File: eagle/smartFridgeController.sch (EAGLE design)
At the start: 12 parts

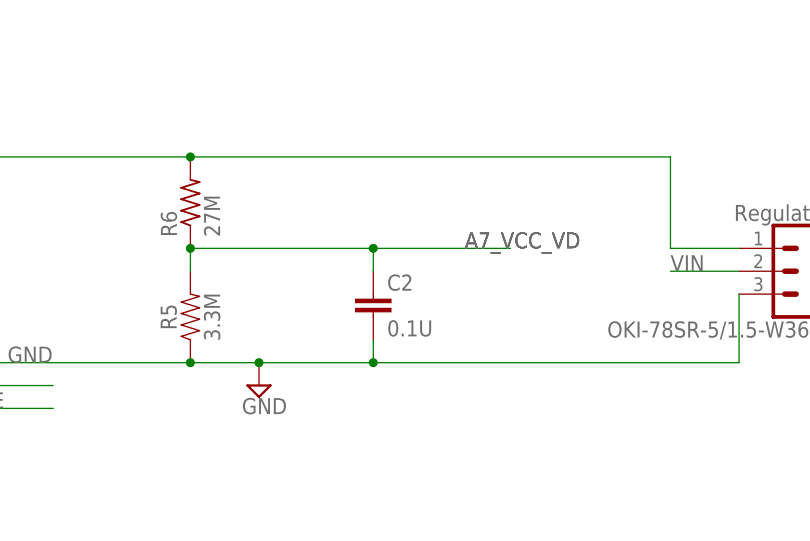
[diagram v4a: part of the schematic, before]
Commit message: silkscreen updates
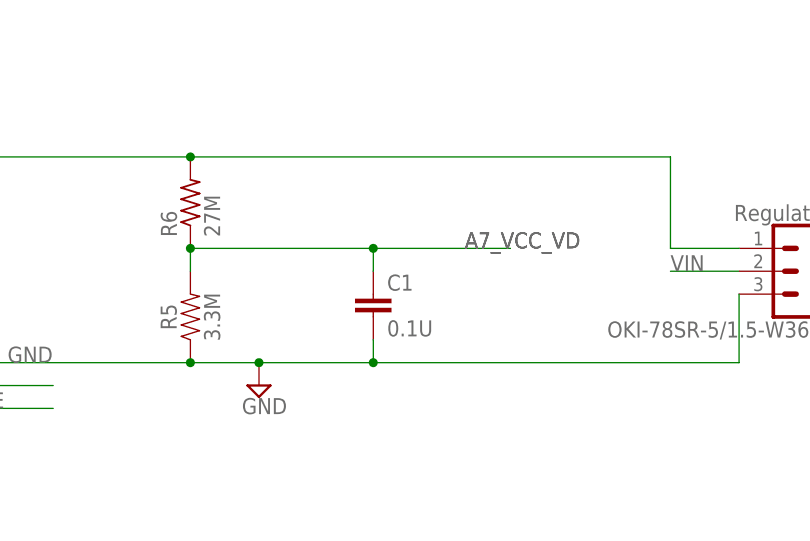
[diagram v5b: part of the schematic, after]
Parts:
- renumbered C2 to C1
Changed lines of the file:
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@@
 <part name="FRAME1" library="SparkFun-Aesthetics" deviceset="FRAME-A4L" device=""/>
 <part name="SUPPLY7" library="supply2" deviceset="GND" device=""/>
-<part name="C2" library="SparkFun-Capacitors" deviceset="0.1UF" device="-KIT-EZ-50V-20%" value="0.1U"/>
+<part name="C1" library="SparkFun-Capacitors" deviceset="0.1UF" device="-KIT-EZ-50V-20%" value="0.1U"/>
 <part name="R5" library="SparkFun-Resistors" deviceset="1KOHM" device="-HORIZ-1/4W-1%" value="3.3M"/>
 <part name="JST" library="SparkFun-Connectors" deviceset="CONN_04" device="JST-PTH"/>
@@
 <instance part="FRAME1" gate="G$1" x="0" y="0"/>
 <instance part="SUPPLY7" gate="GND" x="177.8" y="43.18"/>
-<instance part="C2" gate="G$1" x="190.5" y="50.8"/>
+<instance part="C1" gate="G$1" x="190.5" y="50.8"/>
 <instance part="R5" gate="G$1" x="170.18" y="50.8" rot="R90"/>
 <instance part="JST" gate="G$1" x="139.7" y="43.18"/>
@@
 <net name="GND" class="1">
 <segment>
-<pinref part="C2" gate="G$1" pin="2"/>
+<pinref part="C1" gate="G$1" pin="2"/>
 <wire x1="144.78" y1="45.72" x2="170.18" y2="45.72" width="0.1524" layer="91"/>
 <wire x1="170.18" y1="45.72" x2="177.8" y2="45.72" width="0.1524" layer="91"/>
@@
 </segment>
 <segment>
-<pinref part="C2" gate="G$1" pin="1"/>
+<pinref part="C1" gate="G$1" pin="1"/>
 <pinref part="R5" gate="G$1" pin="2"/>
 <wire x1="190.5" y1="55.88" x2="190.5" y2="58.42" width="0.1524" layer="91"/>

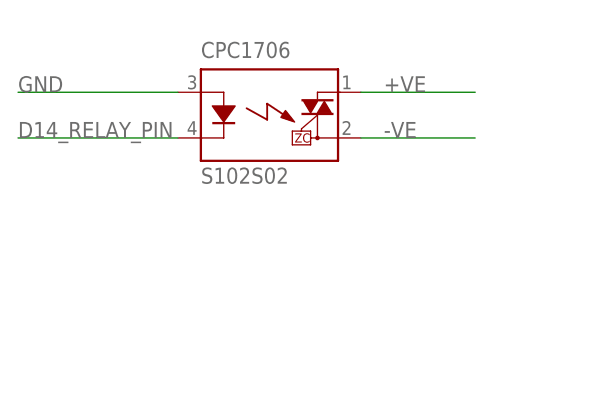
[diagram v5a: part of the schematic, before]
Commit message: Swapped IXYS pins
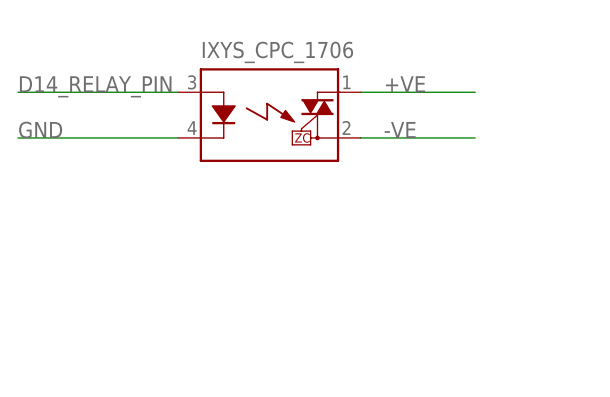
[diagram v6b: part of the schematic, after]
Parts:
- renumbered CPC1706 to IXYS_CPC_1706
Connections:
- net D14_RELAY_PIN: now also IXYS_CPC_1706.A; no longer IXYS_CPC_1706.K
- net GND: now also IXYS_CPC_1706.K; no longer IXYS_CPC_1706.A
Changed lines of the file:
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@@
 <schematic xreflabel="%F%N/%S.%C%R" xrefpart="/%S.%C%R">
 <attributes>
-<attribute name="CNAME" value="MoteinoMega ABoatMon GPS Shield"/>
-<attribute name="CREVISION" value="2.99"/>
+<attribute name="CNAME" value="Smat Fridge Controller"/>
+<attribute name="CREVISION" value="0.2"/>
 <attribute name="DESIGNER" value="greg.cope@gmail.com"/>
 </attributes>
@@
 <part name="SUPPLY3" library="supply2" deviceset="GND" device=""/>
 <part name="OKI-78SR-5/1.5-W36-C" library="SparkFun-Connectors" deviceset="CONN_03" device="" value="Regulator"/>
-<part name="CPC1706" library="relay" library_urn="urn:adsk.eagle:library:339" deviceset="S*02S02" device="" package3d_urn="urn:adsk.eagle:package:24541/1" technology="1"/>
+<part name="IXYS_CPC_1706" library="relay" library_urn="urn:adsk.eagle:library:339" deviceset="S*02S02" device="" package3d_urn="urn:adsk.eagle:package:24541/1" technology="1"/>
 <part name="18B20" library="SparkFun-Connectors" deviceset="CONN_06" device="SILK_FEMALE_PTH"/>
 <part name="DZ1" library="led" library_urn="urn:adsk.eagle:library:259" deviceset="LZR183" device="" package3d_urn="urn:adsk.eagle:package:15788/1"/>
@@
 <instance part="SUPPLY3" gate="GND" x="124.46" y="73.66"/>
 <instance part="OKI-78SR-5/1.5-W36-C" gate="J$1" x="238.76" y="55.88" rot="R180"/>
-<instance part="CPC1706" gate="G$1" x="48.26" y="147.32"/>
+<instance part="IXYS_CPC_1706" gate="G$1" x="48.26" y="147.32" smashed="yes">
+<attribute name="NAME" x="40.64" y="153.67" size="1.778" layer="95" font="vector"/>
+</instance>
 <instance part="18B20" gate="G$1" x="106.68" y="144.78"/>
 <instance part="DZ1" gate="-1" x="228.6" y="121.92" rot="R90"/>
@@
 </segment>
 <segment>
-<pinref part="CPC1706" gate="G$1" pin="A"/>
-<wire x1="38.1" y1="149.86" x2="20.32" y2="149.86" width="0.1524" layer="91"/>
-<label x="20.32" y="149.86" size="1.778" layer="95"/>
-</segment>
-<segment>
 <pinref part="18B20" gate="G$1" pin="4"/>
 <wire x1="111.76" y1="147.32" x2="124.46" y2="147.32" width="0.1524" layer="91"/>
@@
 <wire x1="233.68" y1="147.32" x2="238.76" y2="147.32" width="0.1524" layer="91"/>
 <pinref part="SUPPLY4" gate="GND" pin="GND"/>
+</segment>
+<segment>
+<pinref part="IXYS_CPC_1706" gate="G$1" pin="K"/>
+<wire x1="38.1" y1="144.78" x2="20.32" y2="144.78" width="0.1524" layer="91"/>
+<label x="20.32" y="144.78" size="1.778" layer="95"/>
 </segment>
 </net>
@@
 </segment>
 <segment>
-<pinref part="CPC1706" gate="G$1" pin="DS1"/>
+<pinref part="IXYS_CPC_1706" gate="G$1" pin="DS1"/>
 <wire x1="58.42" y1="149.86" x2="71.12" y2="149.86" width="0.1524" layer="91"/>
 <label x="60.96" y="149.86" size="1.778" layer="95"/>
@@
 </segment>
 <segment>
-<pinref part="CPC1706" gate="G$1" pin="DS2"/>
+<pinref part="IXYS_CPC_1706" gate="G$1" pin="DS2"/>
 <wire x1="58.42" y1="144.78" x2="71.12" y2="144.78" width="0.1524" layer="91"/>
 <label x="60.96" y="144.78" size="1.778" layer="95"/>
@@
 </segment>
 <segment>
-<pinref part="CPC1706" gate="G$1" pin="K"/>
-<wire x1="38.1" y1="144.78" x2="20.32" y2="144.78" width="0.1524" layer="91"/>
-<label x="20.32" y="144.78" size="1.778" layer="95"/>
-</segment>
-</net>
+<pinref part="IXYS_CPC_1706" gate="G$1" pin="A"/>
+<wire x1="38.1" y1="149.86" x2="20.32" y2="149.86" width="0.1524" layer="91"/>
+<label x="20.32" y="149.86" size="1.778" layer="95"/>
+</segment>
+</net>

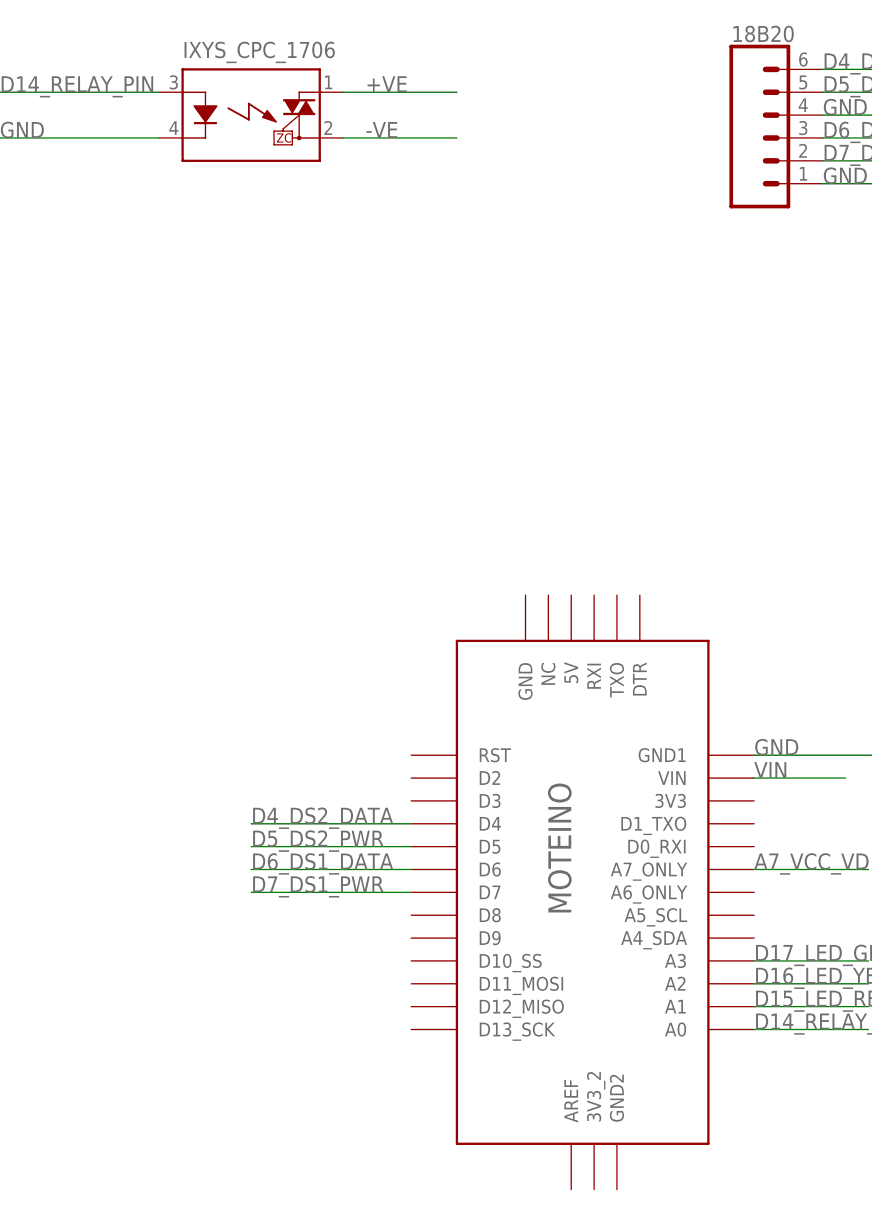
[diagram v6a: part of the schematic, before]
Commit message: Correct SIP package, large footprint
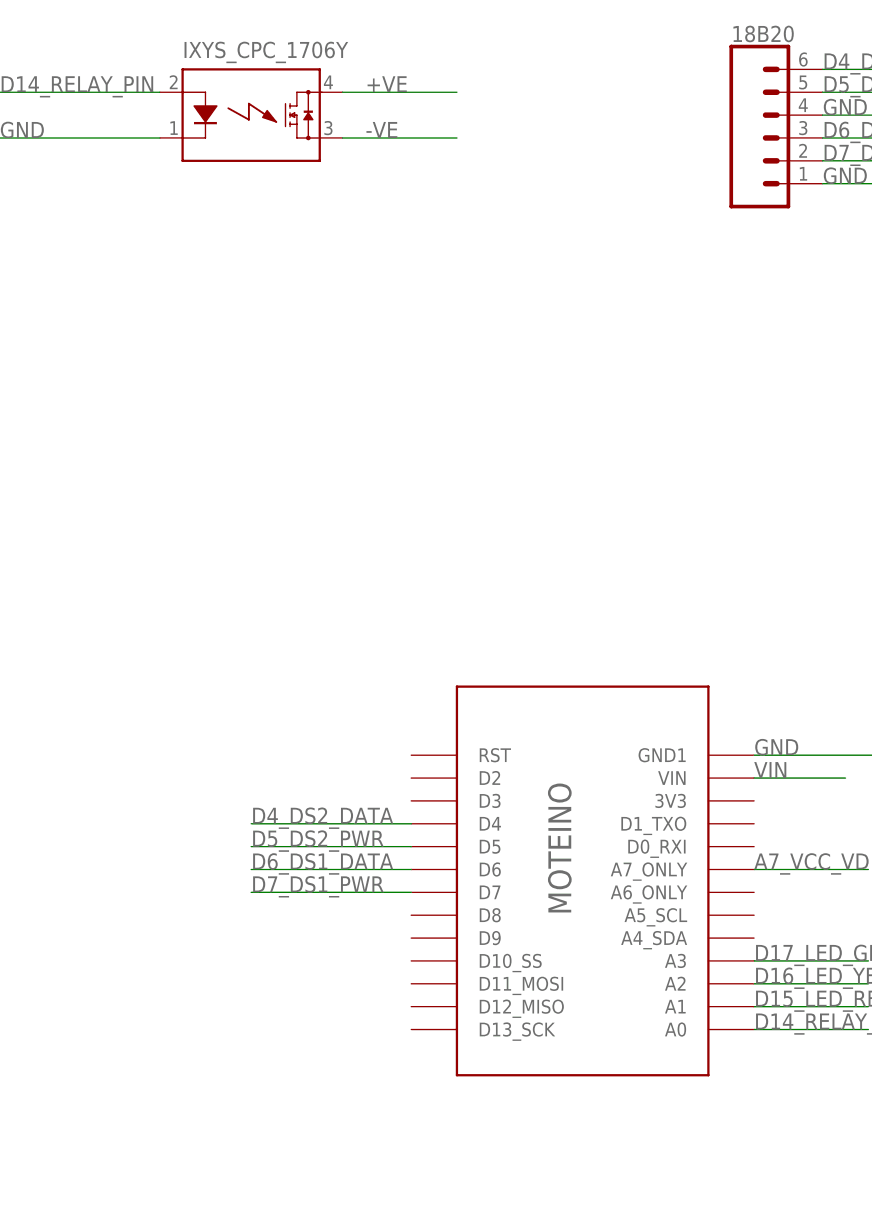
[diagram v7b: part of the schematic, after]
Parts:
- removed IXYS_CPC_1706: S102S02, relay:S102S02
- removed U$1: MOTEINOR6, Moteino:MOTEINOR6
- added IXYS_CPC_1706Y: AQZ102D, relay:AQZ102D
- added U$2: MOTEINO_SIMPLE, Moteino:MOTEINO_SIMPLE
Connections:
- net +VE: now also IXYS_CPC_1706Y.DS1; no longer IXYS_CPC_1706.DS1
- net -VE: now also IXYS_CPC_1706Y.DS2; no longer IXYS_CPC_1706.DS2
- net A7_VCC_VD: now also U$2.A7_ONLY; no longer U$1.A7_ONLY
- net D14_RELAY_PIN: now also IXYS_CPC_1706Y.A, U$2.A0; no longer IXYS_CPC_1706.A, U$1.A0
- net D15_LED_RED_PIN: now also U$2.A1; no longer U$1.A1
- net D16_LED_YELLOW_PIN: now also U$2.A2; no longer U$1.A2
- net D17_LED_GREEN_PIN: now also U$2.A3; no longer U$1.A3
- net D4_DS2_DATA: now also U$2.D4; no longer U$1.D4
- net D5_DS2_PWR: now also U$2.D5; no longer U$1.D5
- net D6_DS1_DATA: now also U$2.D6; no longer U$1.D6
- net D7_DS1_PWR: now also U$2.D7; no longer U$1.D7
- net GND: now also IXYS_CPC_1706Y.K, U$2.GND1; no longer IXYS_CPC_1706.K
- net VIN: now also U$2.VIN; no longer U$1.VIN
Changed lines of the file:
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@@
 <attributes>
 <attribute name="CNAME" value="Smat Fridge Controller"/>
-<attribute name="CREVISION" value="0.2"/>
+<attribute name="CREVISION" value="0.3"/>
 <attribute name="DESIGNER" value="greg.cope@gmail.com"/>
 </attributes>
@@
 <part name="JST" library="SparkFun-Connectors" deviceset="CONN_04" device="JST-PTH"/>
 <part name="R6" library="adafruit" deviceset="R-US_" device="0309/12" value="27M"/>
-<part name="U$1" library="Moteino" deviceset="MOTEINO" device="R6"/>
 <part name="SUPPLY3" library="supply2" deviceset="GND" device=""/>
 <part name="OKI-78SR-5/1.5-W36-C" library="SparkFun-Connectors" deviceset="CONN_03" device="" value="Regulator"/>
-<part name="IXYS_CPC_1706" library="relay" library_urn="urn:adsk.eagle:library:339" deviceset="S*02S02" device="" package3d_urn="urn:adsk.eagle:package:24541/1" technology="1"/>
 <part name="18B20" library="SparkFun-Connectors" deviceset="CONN_06" device="SILK_FEMALE_PTH"/>
 <part name="DZ1" library="led" library_urn="urn:adsk.eagle:library:259" deviceset="LZR183" device="" package3d_urn="urn:adsk.eagle:package:15788/1"/>
@@
 <part name="SUPPLY2" library="supply2" deviceset="GND" device=""/>
 <part name="SUPPLY4" library="supply2" deviceset="GND" device=""/>
+<part name="U$2" library="Moteino" deviceset="MOTEINO_SIMPLE" device=""/>
+<part name="IXYS_CPC_1706Y" library="relay" library_urn="urn:adsk.eagle:library:339" deviceset="AQZ10*D" device="" package3d_urn="urn:adsk.eagle:package:24370/1" technology="2"/>
 </parts>
 <sheets>
@@
 <instance part="JST" gate="G$1" x="139.7" y="43.18"/>
 <instance part="R6" gate="G$1" x="170.18" y="63.5" rot="R90"/>
-<instance part="U$1" gate="G$1" x="81.28" y="58.42"/>
 <instance part="SUPPLY3" gate="GND" x="124.46" y="73.66"/>
 <instance part="OKI-78SR-5/1.5-W36-C" gate="J$1" x="238.76" y="55.88" rot="R180"/>
-<instance part="IXYS_CPC_1706" gate="G$1" x="48.26" y="147.32" smashed="yes">
-<attribute name="NAME" x="40.64" y="153.67" size="1.778" layer="95" font="vector"/>
-</instance>
 <instance part="18B20" gate="G$1" x="106.68" y="144.78"/>
 <instance part="DZ1" gate="-1" x="228.6" y="121.92" rot="R90"/>
@@
 <instance part="SUPPLY2" gate="GND" x="241.3" y="134.62" rot="R90"/>
 <instance part="SUPPLY4" gate="GND" x="241.3" y="147.32" rot="R90"/>
+<instance part="U$2" gate="G$1" x="81.28" y="58.42"/>
+<instance part="IXYS_CPC_1706Y" gate="G$1" x="48.26" y="147.32" smashed="yes">
+<attribute name="NAME" x="40.64" y="153.67" size="1.778" layer="95" font="vector"/>
+</instance>
 </instances>
 <busses>
@@
 <wire x1="124.46" y1="76.2" x2="104.14" y2="76.2" width="0.1524" layer="91"/>
 <label x="104.14" y="76.2" size="1.778" layer="95"/>
+<pinref part="U$2" gate="G$1" pin="GND1"/>
 </segment>
 <segment>
@@
 </segment>
 <segment>
-<pinref part="IXYS_CPC_1706" gate="G$1" pin="K"/>
 <wire x1="38.1" y1="144.78" x2="20.32" y2="144.78" width="0.1524" layer="91"/>
 <label x="20.32" y="144.78" size="1.778" layer="95"/>
+<pinref part="IXYS_CPC_1706Y" gate="G$1" pin="K"/>
 </segment>
 </net>
 <net name="VIN" class="1">
 <segment>
-<pinref part="U$1" gate="G$1" pin="VIN"/>
 <wire x1="104.14" y1="73.66" x2="114.3" y2="73.66" width="0.1524" layer="91"/>
 <label x="104.14" y="73.66" size="1.778" layer="95"/>
+<pinref part="U$2" gate="G$1" pin="VIN"/>
 </segment>
 <segment>
@@
 </segment>
 <segment>
-<pinref part="IXYS_CPC_1706" gate="G$1" pin="DS1"/>
 <wire x1="58.42" y1="149.86" x2="71.12" y2="149.86" width="0.1524" layer="91"/>
 <label x="60.96" y="149.86" size="1.778" layer="95"/>
+<pinref part="IXYS_CPC_1706Y" gate="G$1" pin="DS1"/>
 </segment>
 </net>
@@
 </segment>
 <segment>
-<pinref part="IXYS_CPC_1706" gate="G$1" pin="DS2"/>
 <wire x1="58.42" y1="144.78" x2="71.12" y2="144.78" width="0.1524" layer="91"/>
 <label x="60.96" y="144.78" size="1.778" layer="95"/>
+<pinref part="IXYS_CPC_1706Y" gate="G$1" pin="DS2"/>
 </segment>
 </net>
 <net name="D7_DS1_PWR" class="0">
 <segment>
-<pinref part="U$1" gate="G$1" pin="D7"/>
 <wire x1="66.04" y1="60.96" x2="48.26" y2="60.96" width="0.1524" layer="91"/>
 <label x="48.26" y="60.96" size="1.778" layer="95"/>
+<pinref part="U$2" gate="G$1" pin="D7"/>
 </segment>
 <segment>
@@
 <net name="D6_DS1_DATA" class="0">
 <segment>
-<pinref part="U$1" gate="G$1" pin="D6"/>
 <wire x1="66.04" y1="63.5" x2="48.26" y2="63.5" width="0.1524" layer="91"/>
 <label x="48.26" y="63.5" size="1.778" layer="95"/>
+<pinref part="U$2" gate="G$1" pin="D6"/>
 </segment>
 <segment>
@@
 <net name="D4_DS2_DATA" class="0">
 <segment>
-<pinref part="U$1" gate="G$1" pin="D4"/>
 <wire x1="66.04" y1="68.58" x2="48.26" y2="68.58" width="0.1524" layer="91"/>
 <label x="48.26" y="68.58" size="1.778" layer="95"/>
+<pinref part="U$2" gate="G$1" pin="D4"/>
 </segment>
 <segment>
@@
 <net name="D15_LED_RED_PIN" class="0">
 <segment>
-<pinref part="U$1" gate="G$1" pin="A1"/>
 <wire x1="104.14" y1="48.26" x2="116.84" y2="48.26" width="0.1524" layer="91"/>
 <label x="104.14" y="48.26" size="1.778" layer="95"/>
+<pinref part="U$2" gate="G$1" pin="A1"/>
 </segment>
 <segment>
@@
 <net name="D5_DS2_PWR" class="0">
 <segment>
-<pinref part="U$1" gate="G$1" pin="D5"/>
 <wire x1="66.04" y1="66.04" x2="48.26" y2="66.04" width="0.1524" layer="91"/>
 <label x="48.26" y="66.04" size="1.778" layer="95"/>
+<pinref part="U$2" gate="G$1" pin="D5"/>
 </segment>
 <segment>
@@
 <net name="A7_VCC_VD" class="0">
 <segment>
-<pinref part="U$1" gate="G$1" pin="A7_ONLY"/>
 <wire x1="104.14" y1="63.5" x2="116.84" y2="63.5" width="0.1524" layer="91"/>
 <label x="104.14" y="63.5" size="1.778" layer="95"/>
+<pinref part="U$2" gate="G$1" pin="A7_ONLY"/>
 </segment>
 <segment>
@@
 <net name="D14_RELAY_PIN" class="0">
 <segment>
-<pinref part="U$1" gate="G$1" pin="A0"/>
 <wire x1="104.14" y1="45.72" x2="116.84" y2="45.72" width="0.1524" layer="91"/>
 <label x="104.14" y="45.72" size="1.778" layer="95"/>
-</segment>
-<segment>
-<pinref part="IXYS_CPC_1706" gate="G$1" pin="A"/>
+<pinref part="U$2" gate="G$1" pin="A0"/>
+</segment>
+<segment>
 <wire x1="38.1" y1="149.86" x2="20.32" y2="149.86" width="0.1524" layer="91"/>
 <label x="20.32" y="149.86" size="1.778" layer="95"/>
+<pinref part="IXYS_CPC_1706Y" gate="G$1" pin="A"/>
 </segment>
 </net>
 <net name="D16_LED_YELLOW_PIN" class="0">
 <segment>
-<pinref part="U$1" gate="G$1" pin="A2"/>
 <wire x1="104.14" y1="50.8" x2="116.84" y2="50.8" width="0.1524" layer="91"/>
 <label x="104.14" y="50.8" size="1.778" layer="95"/>
+<pinref part="U$2" gate="G$1" pin="A2"/>
 </segment>
 <segment>
@@
 <net name="D17_LED_GREEN_PIN" class="0">
 <segment>
-<pinref part="U$1" gate="G$1" pin="A3"/>
 <wire x1="104.14" y1="53.34" x2="116.84" y2="53.34" width="0.1524" layer="91"/>
 <label x="104.14" y="53.34" size="1.778" layer="95"/>
-</segment>
-<segment>
+<pinref part="U$2" gate="G$1" pin="A3"/>
+</segment>
+<segment>
